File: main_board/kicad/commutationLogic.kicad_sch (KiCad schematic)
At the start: 9 parts, among them U8 AT28C64B

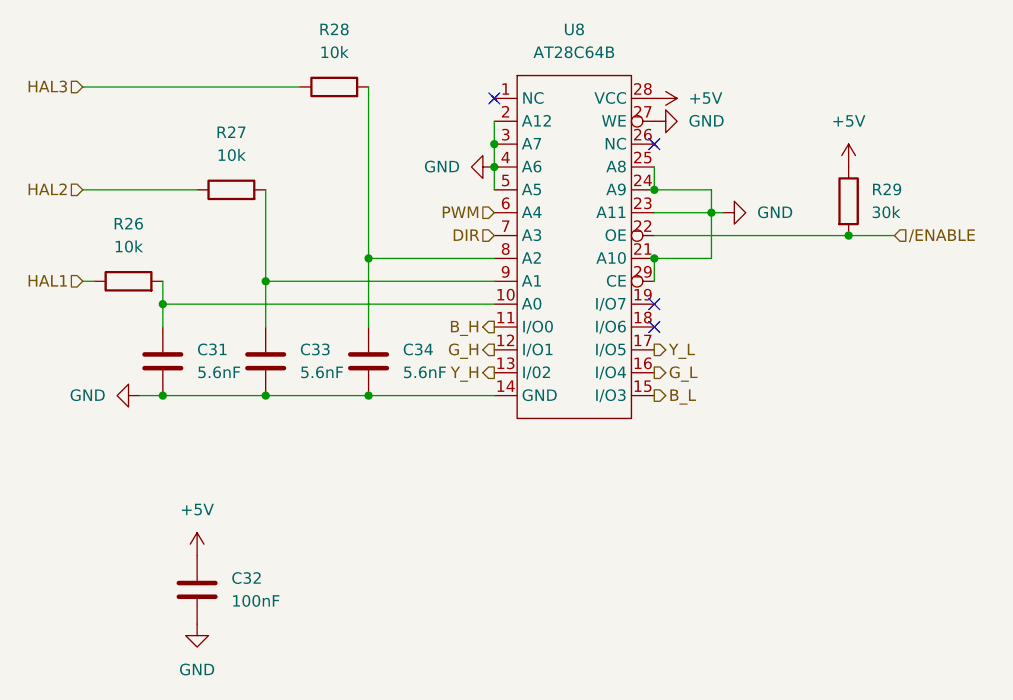
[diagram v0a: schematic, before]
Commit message: resolved ERC
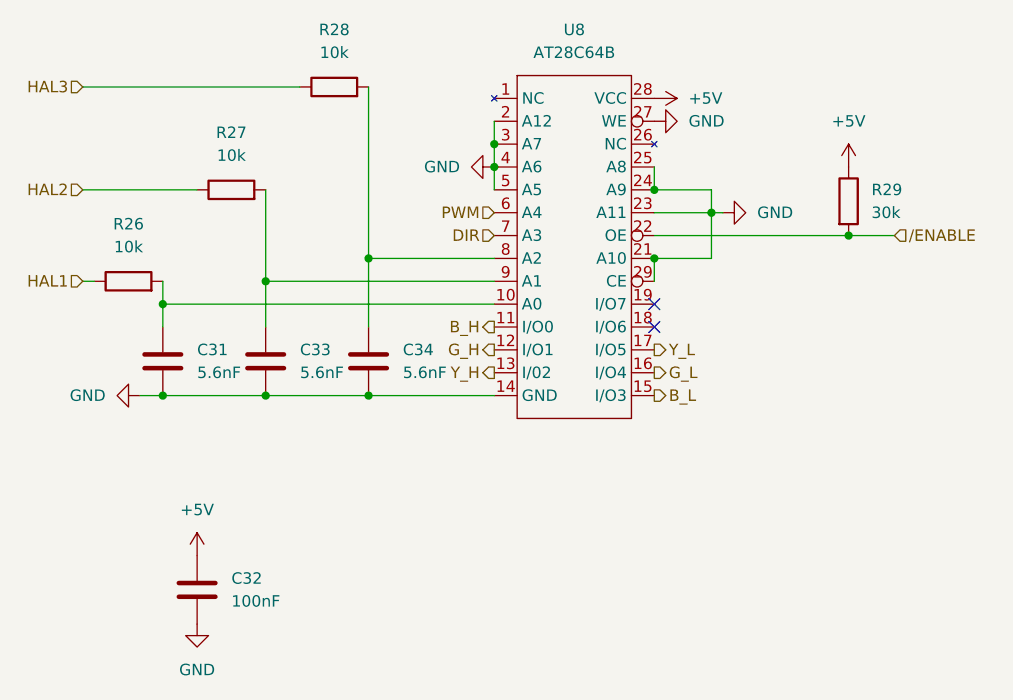
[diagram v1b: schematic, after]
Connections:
- no-connect marks 4 -> 2
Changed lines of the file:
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@@
   (no_connect (at 157.48 109.22))
   (no_connect (at 157.48 106.68))
-  (no_connect (at 139.7 83.82))
-  (no_connect (at 157.48 88.9))
   (wire (pts (xy 93.98 104.14) (xy 95.25 104.14))
     (stroke (width 0) (type default))

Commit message: updated to post review state
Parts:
- removed C33, C34: 5.6nF, symbol Device:C
- removed R26: 10k, symbol Device:R
- removed R29: 30k, symbol Device:R
- added C17, C24: 1.8nF, symbol Device:C
- added R18: 30k, symbol Device:R
- C31: value 5.6nF -> 1.8nF
- R27, R28: value 10k -> 30k
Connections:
- net /ENABLE is gone; now on net GND: U8.22 (OE)
- net +5V: now also U8.27 (WE)
- net GND: now also C17.2, C24.2; no longer U8.27 (WE)
- net HAL1: now also R27.1
- net HAL2: now also R18.1; no longer R27.1
- net at U8.9 (A1): now also C17.1, R18.2; no longer R27.2
- net at C31.1, U8.10 (A0): now also R27.2
- net at R28.2, U8.8 (A2): now also C24.1

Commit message: added footprints
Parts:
- C17, C24, C31: footprint (none) -> Capacitor_THT:C_Disc_D6.0mm_W2.5mm_P5.00mm
- C32: footprint (none) -> Capacitor_THT:C_Disc_D3.0mm_W1.6mm_P2.50mm
- R18, R27, R28: footprint (none) -> Resistor_THT:R_Axial_DIN0207_L6.3mm_D2.5mm_P7.62mm_Horizontal
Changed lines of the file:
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@@
       (effects (font (size 1.27 1.27)) (justify left))
     )
-    (property "Footprint" "" (at 115.2652 116.84 0)
+    (property "Footprint" "Capacitor_THT:C_Disc_D6.0mm_W2.5mm_P5.00mm" (at 115.2652 116.84 0)
       (effects (font (size 1.27 1.27)) hide)
     )
@@
       (effects (font (size 1.27 1.27)))
     )
-    (property "Footprint" "" (at 110.49 95.758 90)
+    (property "Footprint" "Resistor_THT:R_Axial_DIN0207_L6.3mm_D2.5mm_P7.62mm_Horizontal" (at 110.49 95.758 90)
       (effects (font (size 1.27 1.27)) hide)
     )
@@
       (effects (font (size 1.27 1.27)))
     )
-    (property "Footprint" "" (at 121.92 84.328 90)
+    (property "Footprint" "Resistor_THT:R_Axial_DIN0207_L6.3mm_D2.5mm_P7.62mm_Horizontal" (at 121.92 84.328 90)
       (effects (font (size 1.27 1.27)) hide)
     )
@@
       (effects (font (size 1.27 1.27)))
     )
-    (property "Footprint" "" (at 99.06 105.918 90)
+    (property "Footprint" "Resistor_THT:R_Axial_DIN0207_L6.3mm_D2.5mm_P7.62mm_Horizontal" (at 99.06 105.918 90)
       (effects (font (size 1.27 1.27)) hide)
     )
@@
       (effects (font (size 1.27 1.27)) (justify left))
     )
-    (property "Footprint" "" (at 107.6452 142.24 0)
+    (property "Footprint" "Capacitor_THT:C_Disc_D3.0mm_W1.6mm_P2.50mm" (at 107.6452 142.24 0)
       (effects (font (size 1.27 1.27)) hide)
     )
@@
       (effects (font (size 1.27 1.27)) (justify left))
     )
-    (property "Footprint" "" (at 103.8352 116.84 0)
+    (property "Footprint" "Capacitor_THT:C_Disc_D6.0mm_W2.5mm_P5.00mm" (at 103.8352 116.84 0)
       (effects (font (size 1.27 1.27)) hide)
     )
@@
       (effects (font (size 1.27 1.27)) (justify left))
     )
-    (property "Footprint" "" (at 126.6952 116.84 0)
-      (effects (font (size 1.27 1.27)) hide)
-    )
+    (property "Footprint" "Capacitor_THT:C_Disc_D6.0mm_W2.5mm_P5.00mm" (at 126.6952 116.84 0)
+      (effects (font (size 1.27 1.27)) hide)
+    )
